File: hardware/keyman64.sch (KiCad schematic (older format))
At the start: 33 parts, among them J1 POWER, P1 COMPUTER, P2 KEYBOARD, P3 USB, P4 SERIAL, P5 CONTROL, SW1 RESET, SW2 BOOT, U1 CD74HC22106/MT8808, U2 ATMEGA1284P-PU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

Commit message: Hardware: Disconnected Atmega AREF Pin, continued rerouting...
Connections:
- net VCC: no longer U2.32 (AREF)
- no-connect marks 10 -> 11
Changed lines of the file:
@@
 Text Label 4300 7100 0    60   ~ 0
 CD
-Text Label 2300 5100 2    60   ~ 0
-VCC
 Text Label 3100 3600 1    60   ~ 0
 VCC
@@
 	0    -1   -1   0
 $EndComp
+NoConn ~ 2300 5100
 $EndSCHEMATC

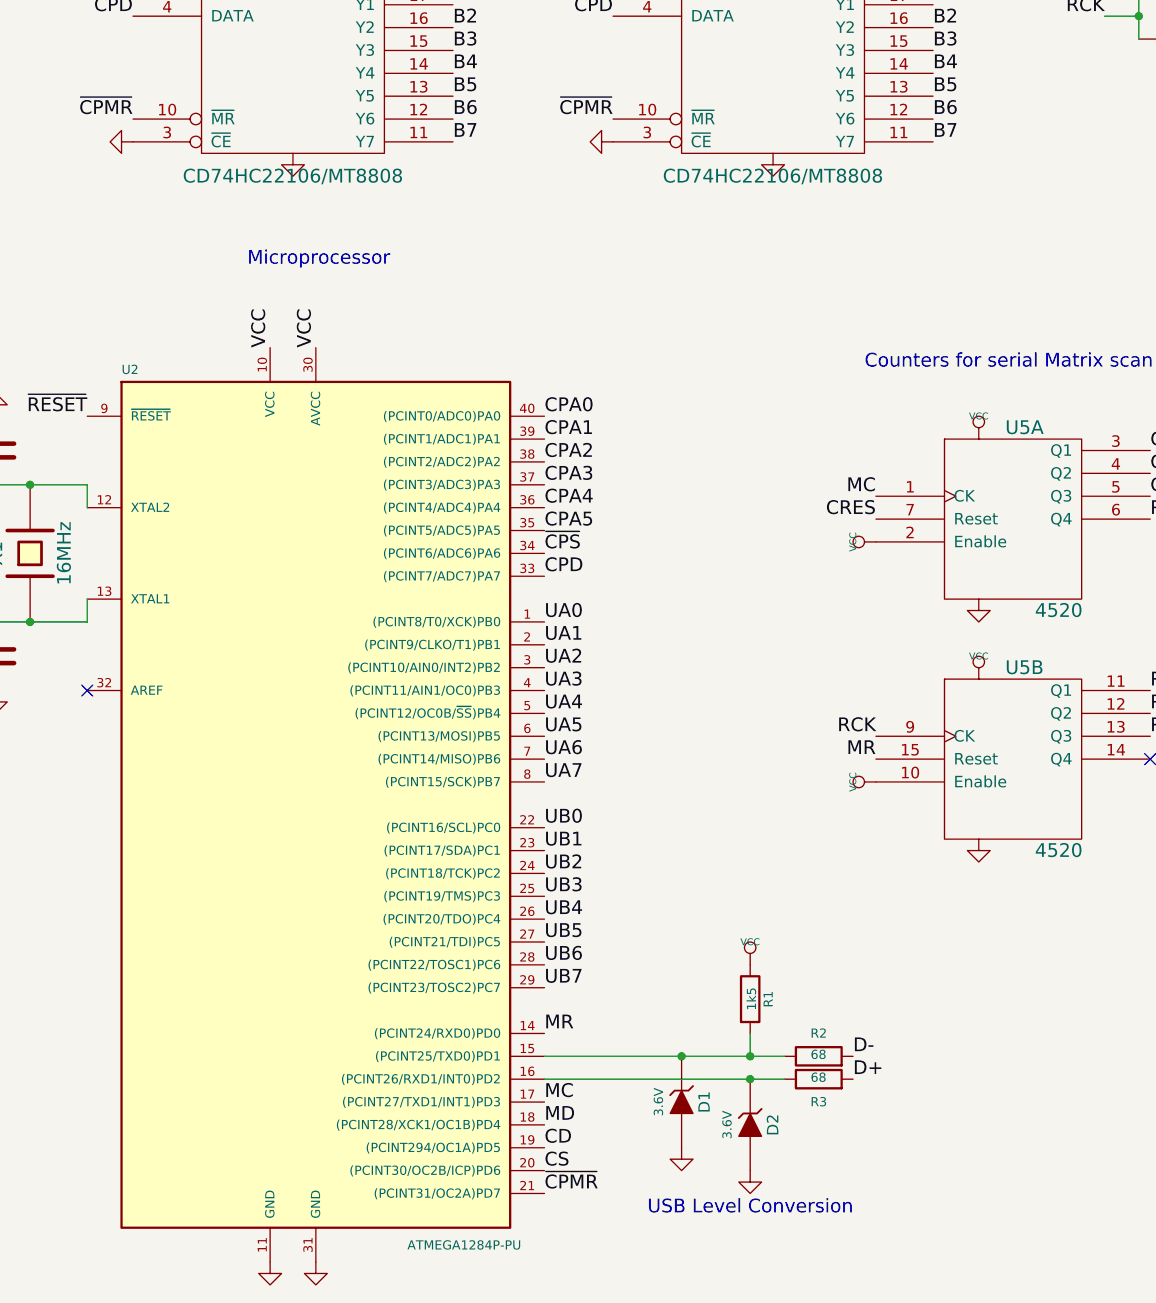
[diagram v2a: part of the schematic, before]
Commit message: Hardware: Fixed wrong USB level conversion circuit
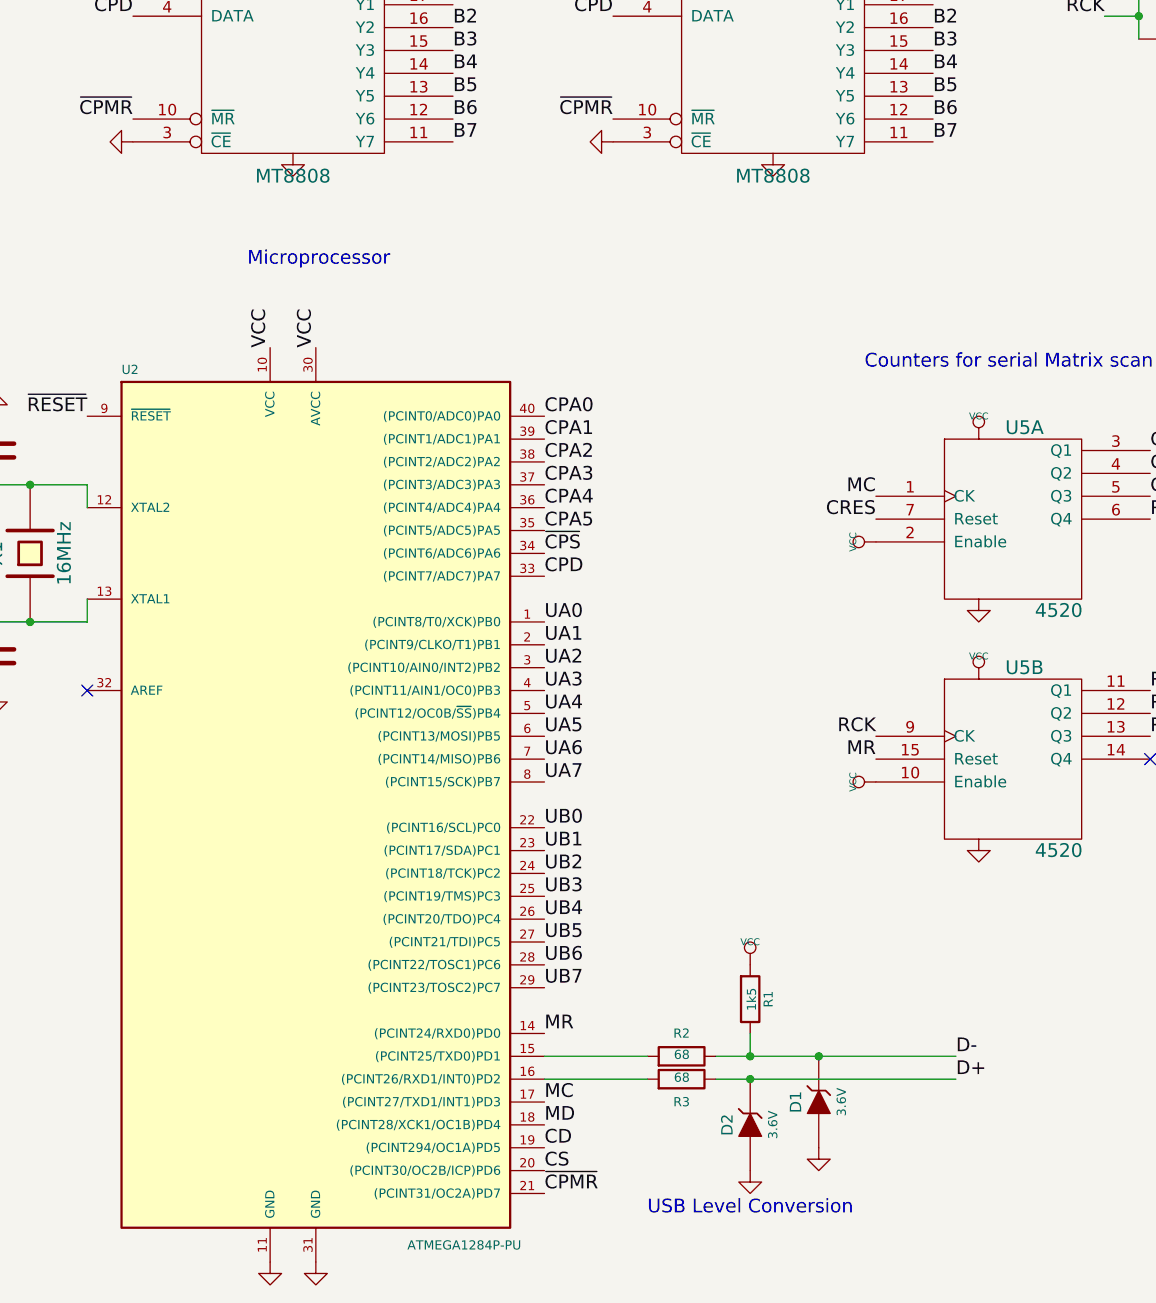
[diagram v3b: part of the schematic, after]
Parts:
- U1, U7: value CD74HC22106/MT8808 -> MT8808
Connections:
- net D+: now also D2.1 (K), R3.1; no longer R3.2
- net D-: now also D1.1 (K), R1.1, R2.1; no longer R2.2
- net VCC: now also R1.2; no longer R1.1
- new net: R2.2, U2.15 ((PCINT25/TXD0)PD1)
- new net: R3.2, U2.16 ((PCINT26/RXD1/INT0)PD2)
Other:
- moved on the sheet: D1, R2, R3
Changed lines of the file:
@@
 Sheet 1 1
 Title "Keyman64 programmable keyboard and hardware controller"
-Date "2016-05-09"
-Rev "3"
+Date "2016-07-25"
+Rev "4"
 Comp "Henning Bekel"
 Comment1 "http://www.henning-bekel.de/keyman64"
@@
 P 3200 1900
 F 0 "U1" H 2850 2800 60  0000 C CNN
-F 1 "CD74HC22106/MT8808" H 3200 950 60  0000 C CNN
+F 1 "MT8808" H 3200 950 60  0000 C CNN
 F 2 "Sockets_DIP:DIP-28__600" H 3150 2600 60  0001 C CNN
 F 3 "" H 3150 2600 60  0000 C CNN
@@
 Text Label 2300 3900 2    60   ~ 0
 ~RESET
-Text Label 5650 6700 0    60   ~ 0
+Text Label 6100 6700 0    60   ~ 0
 D-
-Text Label 5650 6800 0    60   ~ 0
+Text Label 6100 6800 0    60   ~ 0
 D+
 Text Label 4300 4800 0    60   ~ 0
@@
 L R R2
 U 1 1 55B38786
-P 5500 6700
-F 0 "R2" V 5600 6700 40  0000 C CNN
-F 1 "68" V 5507 6701 40  0000 C CNN
-F 2 "Discret:R1" V 5430 6700 30  0001 C CNN
-F 3 "" H 5500 6700 30  0000 C CNN
-	1    5500 6700
-	0    -1   -1   0
+P 4900 6700
+F 0 "R2" V 5000 6700 40  0000 C CNN
+F 1 "68" V 4907 6701 40  0000 C CNN
+F 2 "Discret:R1" V 4830 6700 30  0001 C CNN
+F 3 "" H 4900 6700 30  0000 C CNN
+	1    4900 6700
+	0    1    -1   0
 $EndComp
 $Comp
 L R R3
 U 1 1 55B38798
-P 5500 6800
-F 0 "R3" V 5400 6800 40  0000 C CNN
-F 1 "68" V 5507 6801 40  0000 C CNN
-F 2 "Discret:R1" V 5430 6800 30  0001 C CNN
-F 3 "" H 5500 6800 30  0000 C CNN
-	1    5500 6800
-	0    -1   -1   0
+P 4900 6800
+F 0 "R3" V 4800 6800 40  0000 C CNN
+F 1 "68" V 4907 6801 40  0000 C CNN
+F 2 "Discret:R1" V 4830 6800 30  0001 C CNN
+F 3 "" H 4900 6800 30  0000 C CNN
+	1    4900 6800
+	0    1    -1   0
 $EndComp
 $Comp
@@
 F 3 "" H 5200 6450 30  0000 C CNN
 	1    5200 6450
-	1    0    0    -1
+	1    0    0    1
 $EndComp
 $Comp
@@
 F 3 "" H 5200 7000 60  0000 C CNN
 	1    5200 7000
-	0    1    1    0
+	0    -1   1    0
 $EndComp
 $Comp
 L ZENER D1
 U 1 1 55B387E1
-P 4900 6900
-F 0 "D1" H 4900 7000 50  0000 C CNN
-F 1 "3.6V" H 4900 6800 40  0000 C CNN
-F 2 "Diode:Diode-2.5mm-Vertical" H 4900 6900 60  0001 C CNN
-F 3 "" H 4900 6900 60  0000 C CNN
-	1    4900 6900
-	0    1    1    0
+P 5500 6900
+F 0 "D1" H 5500 7000 50  0000 C CNN
+F 1 "3.6V" H 5500 6800 40  0000 C CNN
+F 2 "Diode:Diode-2.5mm-Vertical" H 5500 6900 60  0001 C CNN
+F 3 "" H 5500 6900 60  0000 C CNN
+	1    5500 6900
+	0    -1   1    0
 $EndComp
 $Comp
@@
 F 3 "" H 5200 6300 60  0000 C CNN
 	1    5200 6300
-	1    0    0    -1
+	-1   0    0    -1
 $EndComp
 $Comp
@@
 F 3 "" H 5200 7200 60  0000 C CNN
 	1    5200 7200
-	1    0    0    -1
+	-1   0    0    -1
 $EndComp
 $Comp
 L GND #PWR032
 U 1 1 55B38825
-P 4900 7100
-F 0 "#PWR032" H 4900 7100 30  0001 C CNN
-F 1 "GND" H 4900 7030 30  0001 C CNN
-F 2 "" H 4900 7100 60  0000 C CNN
-F 3 "" H 4900 7100 60  0000 C CNN
-	1    4900 7100
-	1    0    0    -1
+P 5500 7100
+F 0 "#PWR032" H 5500 7100 30  0001 C CNN
+F 1 "GND" H 5500 7030 30  0001 C CNN
+F 2 "" H 5500 7100 60  0000 C CNN
+F 3 "" H 5500 7100 60  0000 C CNN
+	1    5500 7100
+	-1   0    0    -1
 $EndComp
 Text Notes 4750 7400 0    60   ~ 0
@@
 Connection ~ 2050 4800
 Wire Wire Line
-	4300 6700 5350 6700
-Connection ~ 4900 6700
-Wire Wire Line
-	4300 6800 5350 6800
+	6100 6700 5050 6700
+Connection ~ 5500 6700
+Wire Wire Line
+	6100 6800 5050 6800
 Wire Wire Line
 	5200 6700 5200 6600
@@
 P 5300 1900
 F 0 "U7" H 4950 2800 60  0000 C CNN
-F 1 "CD74HC22106/MT8808" H 5300 950 60  0000 C CNN
+F 1 "MT8808" H 5300 950 60  0000 C CNN
 F 2 "Sockets:PLCC28" H 5250 2600 60  0001 C CNN
 F 3 "" H 5250 2600 60  0000 C CNN
@@
 $EndComp
 NoConn ~ 2300 5100
+Wire Wire Line
+	4750 6700 4300 6700
+Wire Wire Line
+	4750 6800 4300 6800
 $EndSCHEMATC

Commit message: Hardware: Placed resistors and diodes horizontally
This allows to assemble the board as flat as possible in case there is not
much height clearance for installation.
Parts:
- D1, D2: footprint Diode:Diode-2.5mm-Vertical -> Diode:D3
- R1, R2, R3: footprint Discret:R1 -> Discret:R3
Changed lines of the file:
@@
 F 0 "R2" V 5000 6700 40  0000 C CNN
 F 1 "68" V 4907 6701 40  0000 C CNN
-F 2 "Discret:R1" V 4830 6700 30  0001 C CNN
+F 2 "Discret:R3" V 4830 6700 30  0001 C CNN
 F 3 "" H 4900 6700 30  0000 C CNN
 	1    4900 6700
@@
 F 0 "R3" V 4800 6800 40  0000 C CNN
 F 1 "68" V 4907 6801 40  0000 C CNN
-F 2 "Discret:R1" V 4830 6800 30  0001 C CNN
+F 2 "Discret:R3" V 4830 6800 30  0001 C CNN
 F 3 "" H 4900 6800 30  0000 C CNN
 	1    4900 6800
@@
 F 0 "R1" V 5280 6450 40  0000 C CNN
 F 1 "1k5" V 5207 6451 40  0000 C CNN
-F 2 "Discret:R1" V 5130 6450 30  0001 C CNN
+F 2 "Discret:R3" V 5130 6450 30  0001 C CNN
 F 3 "" H 5200 6450 30  0000 C CNN
 	1    5200 6450
@@
 F 0 "D2" H 5200 7100 50  0000 C CNN
 F 1 "3.6V" H 5200 6900 40  0000 C CNN
-F 2 "Diode:Diode-2.5mm-Vertical" H 5200 7000 60  0001 C CNN
+F 2 "Diode:D3" H 5200 7000 60  0001 C CNN
 F 3 "" H 5200 7000 60  0000 C CNN
 	1    5200 7000
@@
 F 0 "D1" H 5500 7000 50  0000 C CNN
 F 1 "3.6V" H 5500 6800 40  0000 C CNN
-F 2 "Diode:Diode-2.5mm-Vertical" H 5500 6900 60  0001 C CNN
+F 2 "Diode:D3" H 5500 6900 60  0001 C CNN
 F 3 "" H 5500 6900 60  0000 C CNN
 	1    5500 6900
@@
 	-1   0    0    1
 $EndComp
-Wire Wire Line
-	10350 3050 10350 3150
-Wire Wire Line
-	10650 3050 10650 3200
-Wire Wire Line
-	8250 1750 8100 1750
-Wire Wire Line
-	8100 1750 8100 1500
-Wire Wire Line
-	8100 2150 8100 1950
-Wire Wire Line
-	8100 1950 8250 1950
-Wire Wire Line
-	6900 1400 6900 1600
-Wire Wire Line
-	6900 2050 6900 2250
-Wire Wire Line
-	6900 1500 6800 1500
-Connection ~ 6900 1500
-Wire Wire Line
-	6750 2150 6900 2150
-Connection ~ 6900 2150
-Wire Wire Line
-	2300 4800 2300 4700
-Wire Wire Line
-	1900 4800 2300 4800
-Wire Wire Line
-	2300 4200 2300 4300
-Wire Wire Line
-	1900 4200 2300 4200
-Connection ~ 2050 4200
-Connection ~ 2050 4800
-Wire Wire Line
-	6100 6700 5050 6700
-Connection ~ 5500 6700
-Wire Wire Line
-	6100 6800 5050 6800
-Wire Wire Line
-	5200 6700 5200 6600
-Connection ~ 5200 6700
-Connection ~ 5200 6800
 Text Label 6000 1100 0    60   ~ 0
 A0
@@
 NoConn ~ 2300 5100
 Wire Wire Line
+	10350 3050 10350 3150
+Wire Wire Line
+	10650 3050 10650 3200
+Wire Wire Line
+	8250 1750 8100 1750
+Wire Wire Line
+	8100 1750 8100 1500
+Wire Wire Line
+	8100 2150 8100 1950
+Wire Wire Line
+	8100 1950 8250 1950
+Wire Wire Line
+	6900 1400 6900 1600
+Wire Wire Line
+	6900 2050 6900 2250
+Wire Wire Line
+	6900 1500 6800 1500
+Connection ~ 6900 1500
+Wire Wire Line
+	6750 2150 6900 2150
+Connection ~ 6900 2150
+Wire Wire Line
+	2300 4800 2300 4700
+Wire Wire Line
+	1900 4800 2300 4800
+Wire Wire Line
+	2300 4200 2300 4300
+Wire Wire Line
+	1900 4200 2300 4200
+Connection ~ 2050 4200
+Connection ~ 2050 4800
+Wire Wire Line
+	6100 6700 5050 6700
+Connection ~ 5500 6700
+Wire Wire Line
+	6100 6800 5050 6800
+Connection ~ 5200 6700
+Connection ~ 5200 6800
+Wire Wire Line
 	4750 6700 4300 6700
 Wire Wire Line
 	4750 6800 4300 6800
+Wire Wire Line
+	5200 6700 5200 6600
 $EndSCHEMATC

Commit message: Hardware: Using correct button footprints, rerouted
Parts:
- SW1, SW2: footprint Buttons_Switches_ThroughHole:SW_PUSH_SMALL -> Diode:Button
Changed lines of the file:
@@
 F 0 "SW1" H 10650 1760 50  0000 C CNN
 F 1 "RESET" H 10500 1570 50  0000 C CNN
-F 2 "Buttons_Switches_ThroughHole:SW_PUSH_SMALL" H 10500 1650 60  0001 C CNN
+F 2 "Diode:Button" H 10500 1650 60  0001 C CNN
 F 3 "" H 10500 1650 60  0000 C CNN
 	1    10500 1650
@@
 F 0 "SW2" H 10650 2110 50  0000 C CNN
 F 1 "BOOT" H 10500 1920 50  0000 C CNN
-F 2 "Buttons_Switches_ThroughHole:SW_PUSH_SMALL" H 10500 2000 60  0001 C CNN
+F 2 "Diode:Button" H 10500 2000 60  0001 C CNN
 F 3 "" H 10500 2000 60  0000 C CNN
 	1    10500 2000
